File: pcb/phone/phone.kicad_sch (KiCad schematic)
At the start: 27 parts, among them CN1 S2B-PH-SM4-TB, U4 TPS63021DSJR, U5 TPS7A0218PDBVR, U6 MCP73831-2ACI/MC, U7 MAX17048G+T10

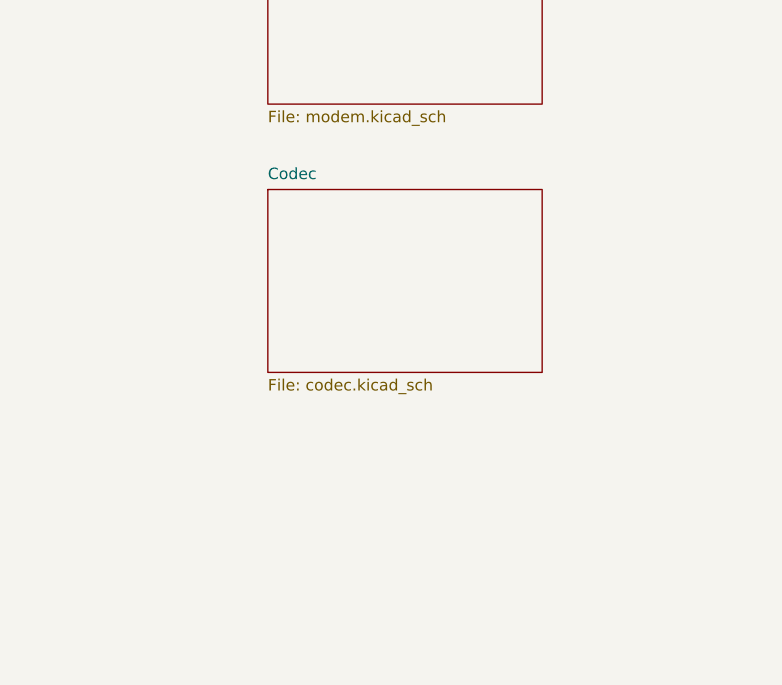
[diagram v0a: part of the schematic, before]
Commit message: Phase 3.4-3.8: Add codec, display, keypad sheets + cleanup temp files
- codec.kicad_sch: ALC5651 codec, I2S level shifter, audio transducers
- display.kicad_sch: main + outer display ZIF connectors, hinge flex
- keypad.kicad_sch: 5x4 tactile switch matrix (20 switches)
- phone.kicad_sch: added Codec, Display, Keypad sheet boxes
- .gitignore: add ERC reports, kicad-cli output, MCP working files
- Removed committed temp files (erc_*.txt, kicad_*.txt, output/)

Generated with [Devin](https://devin.ai)

Co-Authored-By: Devin <158243242+devin-ai-integration[bot]@users.noreply.github.com>
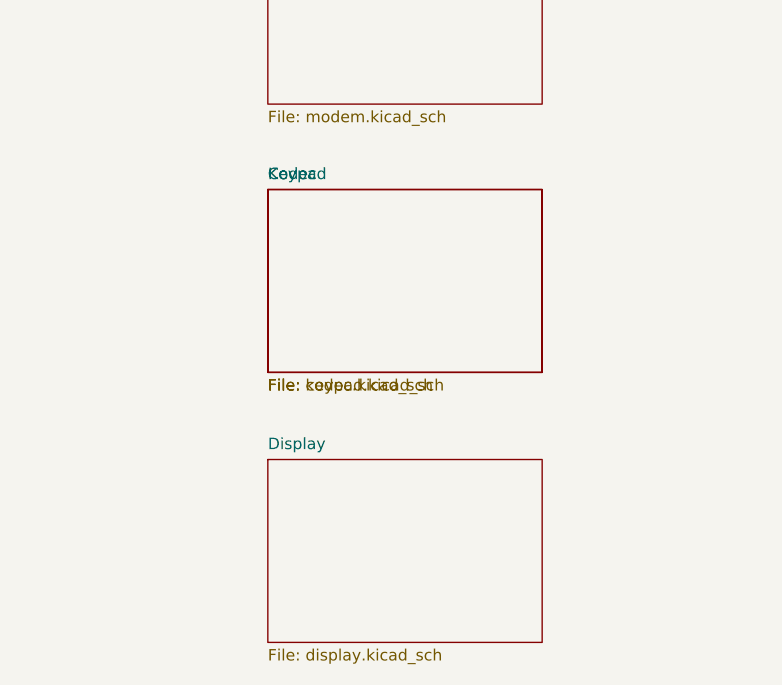
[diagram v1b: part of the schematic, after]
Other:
- added sheet Display (display.kicad_sch)
- added sheet Keypad (keypad.kicad_sch)
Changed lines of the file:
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@@
+		)
+	)
+	(sheet
+		(at 254 280)
+		(size 30.48 20.32)
+		(exclude_from_sim no)
+		(in_bom yes)
+		(on_board yes)
+		(dnp no)
+		(fields_autoplaced yes)
+		(stroke
+			(width 0.1524)
+			(type solid)
+		)
+		(fill
+			(color 0 0 0 0)
+		)
+		(property "Sheetname" "Keypad"
+			(at 254 279 0)
+			(show_name no)
+			(do_not_autoplace no)
+			(effects
+				(font
+					(size 1.27 1.27)
+				)
+				(justify left bottom)
+			)
+		)
+		(property "Sheetfile" "keypad.kicad_sch"
+			(at 254 301 0)
+			(show_name no)
+			(do_not_autoplace no)
+			(effects
+				(font
+					(size 1.27 1.27)
+				)
+				(justify left top)
+			)
+		)
+		(instances
+			(project "phone"
+				(path "/451c3b43-1616-42cb-bf96-d436f4db82c2"
+					(page "4")
+				)
+			)
+		)
+	)
+	(sheet
+		(at 254 310)
+		(size 30.48 20.32)
+		(exclude_from_sim no)
+		(in_bom yes)
+		(on_board yes)
+		(dnp no)
+		(fields_autoplaced yes)
+		(stroke
+			(width 0.1524)
+			(type solid)
+		)
+		(fill
+			(color 0 0 0 0)
+		)
+		(property "Sheetname" "Display"
+			(at 254 309 0)
+			(show_name no)
+			(do_not_autoplace no)
+			(effects
+				(font
+					(size 1.27 1.27)
+				)
+				(justify left bottom)
+			)
+		)
+		(property "Sheetfile" "display.kicad_sch"
+			(at 254 331 0)
+			(show_name no)
+			(do_not_autoplace no)
+			(effects
+				(font
+					(size 1.27 1.27)
+				)
+				(justify left top)
+			)
+		)
+		(instances
+			(project "phone"
+				(path "/451c3b43-1616-42cb-bf96-d436f4db82c2"
+					(page "5")
+				)
+			)
 		)
 	)
